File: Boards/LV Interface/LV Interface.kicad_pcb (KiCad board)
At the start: 4 copper layers, 16 parts, among them J1 Ampseal_35_VT, J10 MM_M_VT_20, J11 MicroFit_VT_4, J2 Ampseal_14_VT, J3 MicroFit_VT_4, J4 MM_M_VT_20, J5 MicroFit_VT_4, J6 MM_M_VT_20, J7 MM_M_VT_20, J8 UF_2_VT, J9 MM_M_VT_20, K1 G5Q-1A4-DC5-5V, U1 RJ45_VT, U2 Fuse_Holder_Blade, U3 Fuse_Holder_Blade

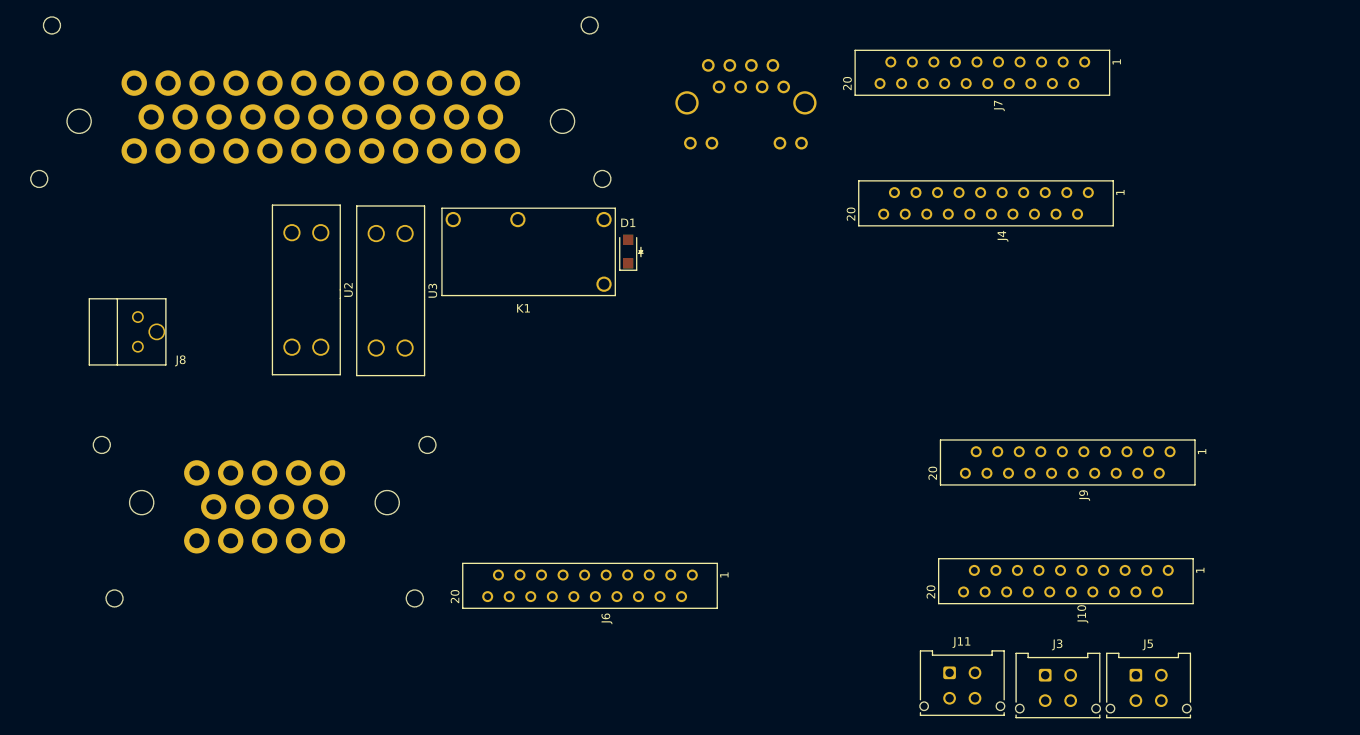
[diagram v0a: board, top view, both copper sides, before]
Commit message: Saving Ampeseal orientations
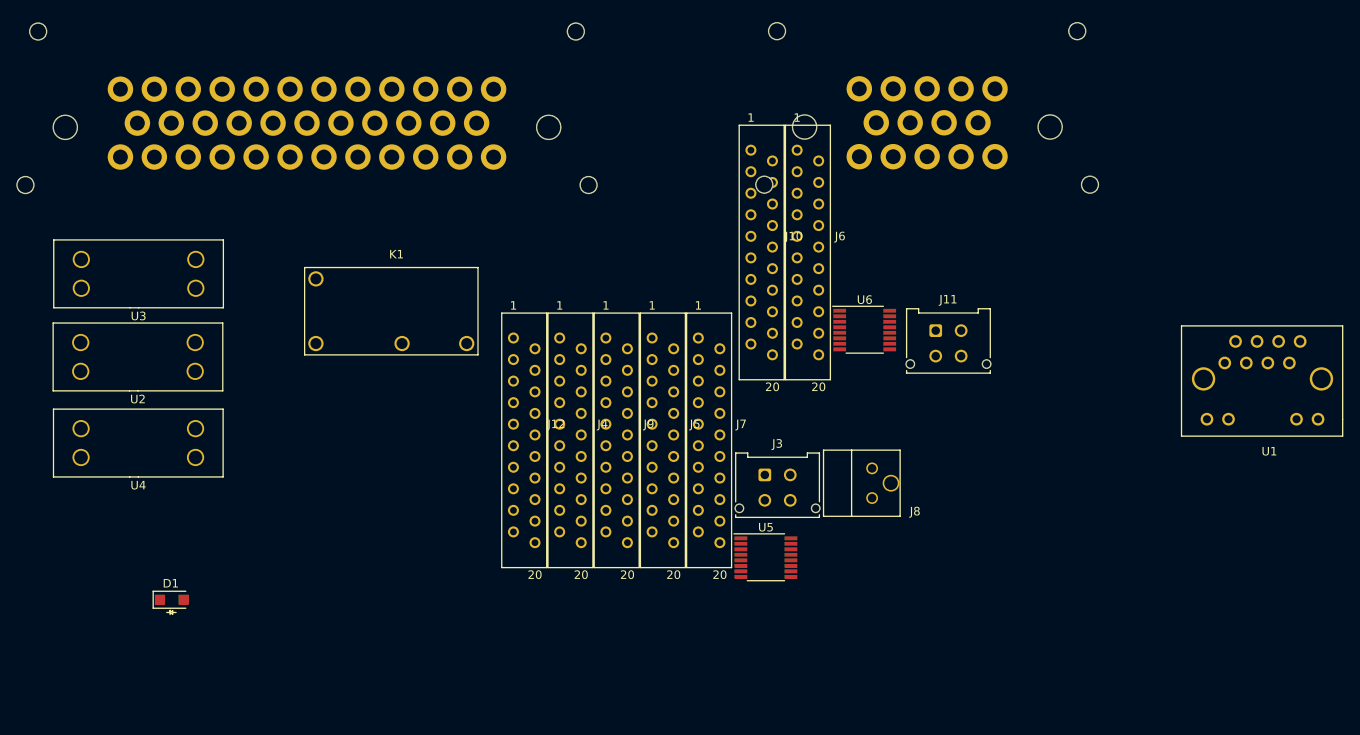
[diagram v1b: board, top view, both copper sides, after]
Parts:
- added J12: MM_F_RA_20, footprints:micromatch_female_ra_20, F.Cu at (76.5, 62.0)
- added U4: Fuse_Holder_Blade, footprints:Fuse_Block_Holder, F.Cu at (32.2, 69.3)
- added U5: INA260, Package_SO:TSSOP-16_4.4x5mm_P0.65mm, F.Cu at (106.2, 82.8)
- added U6: INA260, Package_SO:TSSOP-16_4.4x5mm_P0.65mm, F.Cu at (117.9, 55.9)
- J5: value MicroFit_VT_4 -> MM_F_RA_20; footprint footprints:MicroFit_VT_4 -> footprints:micromatch_female_ra_20
- U1: moved to F.Cu
- moved J2 115.9 mm to (139.7, 32.0), turned to 180 degrees
- moved J8 88.4 mm to (118.7, 72.2)
- moved D1 67.7 mm to (36.2, 87.7), turned to 0 degrees
- moved J5 66.8 mm to (92.8, 62.0)
- moved J10 62.6 mm to (104.5, 39.8), turned to 0 degrees
- moved J9 62.0 mm to (87.4, 62.0), turned to 0 degrees
- moved J4 61.4 mm to (81.9, 62.0), turned to 0 degrees
- moved U1 57.8 mm to (158.2, 66.4), turned to 0 degrees
- moved J7 55.3 mm to (98.3, 62.0), turned to 0 degrees
- moved J6 48.3 mm to (109.9, 39.8), turned to 0 degrees
- moved J3 40.6 mm to (106.1, 73.0)
- moved J11 40.4 mm to (126.2, 56.0)
- moved K1 37.0 mm to (53.2, 57.5), turned to 0 degrees
- moved U3 29.8 mm to (32.3, 49.3), turned to 0 degrees
- moved U2 21.4 mm to (32.2, 59.1), turned to 0 degrees
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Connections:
- D1 pad 1: Net-(D1-Pad1) -> /12V
- J1 pad 3: /MC PRESSURE + -> /EXTRA TEMP 1 +
- J1 pad 30: GND -> /12V_Cooling
- J1 pad 4: /MC PRESSURE SENSE -> /EXTRA TEMP 1 -
- J1 pad 5: /MC PRESSURE - -> /EXTRA TEMP 2 +
- J1 pad 6: /PUMP PRESSURE + -> /EXTRA TEMP 2 -
- J1 pad 7: /PUMP PRESSURE SENSE -> /EXTRA TEMP 3 +
- J1 pad 8: /PUMP PRESSURE - -> /EXTRA TEMP 3 -
- J2 pad 10: /RADIATOR TEMP + -> /CAN HIGH
- J2 pad 11: /RADIATOR TEMP SENSE -> /CAN LOW
- J2 pad 12: /RADIATOR TEMP - -> GND
- J2 pad 2: /MOTOR TEMP SENSE -> /MOTOR TEMP -
- J2 pad 3: /MOTOR TEMP - -> /EXTRA TEMP 4 +
- J2 pad 4: /CAN HIGH -> /EXTRA TEMP 4 -
- J2 pad 5: /CAN LOW -> GND
- J2 pad 7: /MC TEMP SENSE -> /MC TEMP -
- J2 pad 8: /MC TEMP - -> /RADIATOR TEMP +
- J2 pad 9: GND -> /RADIATOR TEMP -
- J3 pad 1: /12V -> GND
- J3 pad 2: GND -> /12V
- J5 pad 1: /12V -> GND
- J5 pad 2: GND -> /12V
- J5 pad 3: /CAN HIGH -> /5V_GLV
- J5 pad 4: /CAN LOW -> /CAN HIGH
- J6 pad 10: /MOTOR TEMP SENSE -> /MC TEMP +
- J6 pad 11: /MOTOR TEMP - -> /MC TEMP -
- J6 pad 12: /PUMP PRESSURE + -> /EXTRA TEMP 1 +
- J6 pad 13: /PUMP PRESSURE SENSE -> /EXTRA TEMP 1 -
- J6 pad 14: /PUMP PRESSURE - -> /EXTRA TEMP 2 +
- J6 pad 15: /MC TEMP + -> /EXTRA TEMP 2 -
- J6 pad 16: /MC TEMP SENSE -> /EXTRA TEMP 3 +
- J6 pad 17: /MC TEMP - -> /EXTRA TEMP 3 -
- J6 pad 18: /MC PRESSURE + -> /EXTRA TEMP 4 +
- J6 pad 19: /MC PRESSURE SENSE -> /EXTRA TEMP 4 -
- J6 pad 20: /MC PRESSURE - -> GND
- J6 pad 7: /RADIATOR TEMP SENSE -> /RADIATOR TEMP -
- J6 pad 8: /RADIATOR TEMP - -> /MOTOR TEMP +
- J6 pad 9: /MOTOR TEMP + -> /MOTOR TEMP -
- K1 pad 5: Net-(D1-Pad1) -> /12V
- U2 pad 2: /12V -> /12V_Fused
